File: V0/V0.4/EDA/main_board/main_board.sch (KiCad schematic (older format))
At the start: 24 parts, among them U1 top_rail_v2, U2 DS3231M, U3 INA219AxD, U5 KA78M05_TO252

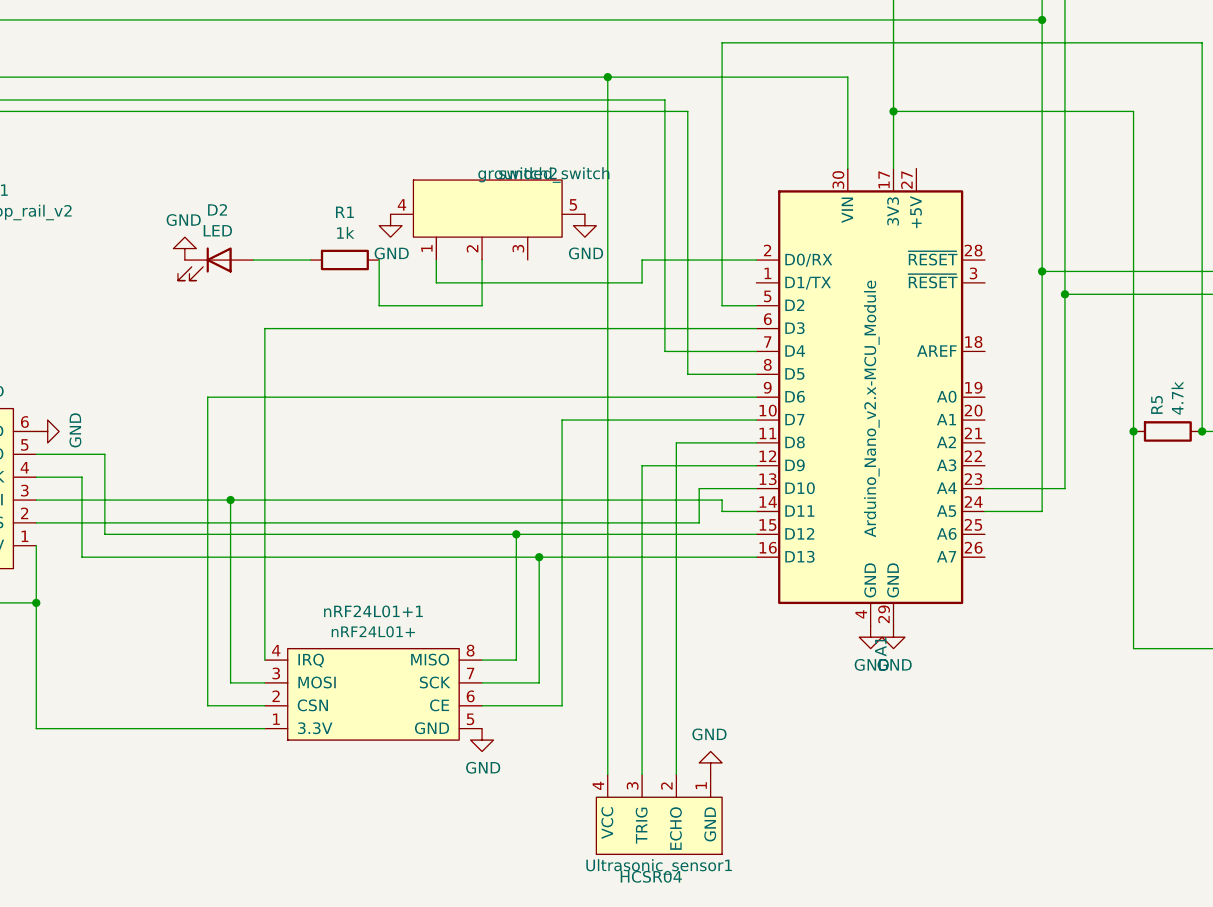
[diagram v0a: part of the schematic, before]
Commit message: update magnet_toggle.ino
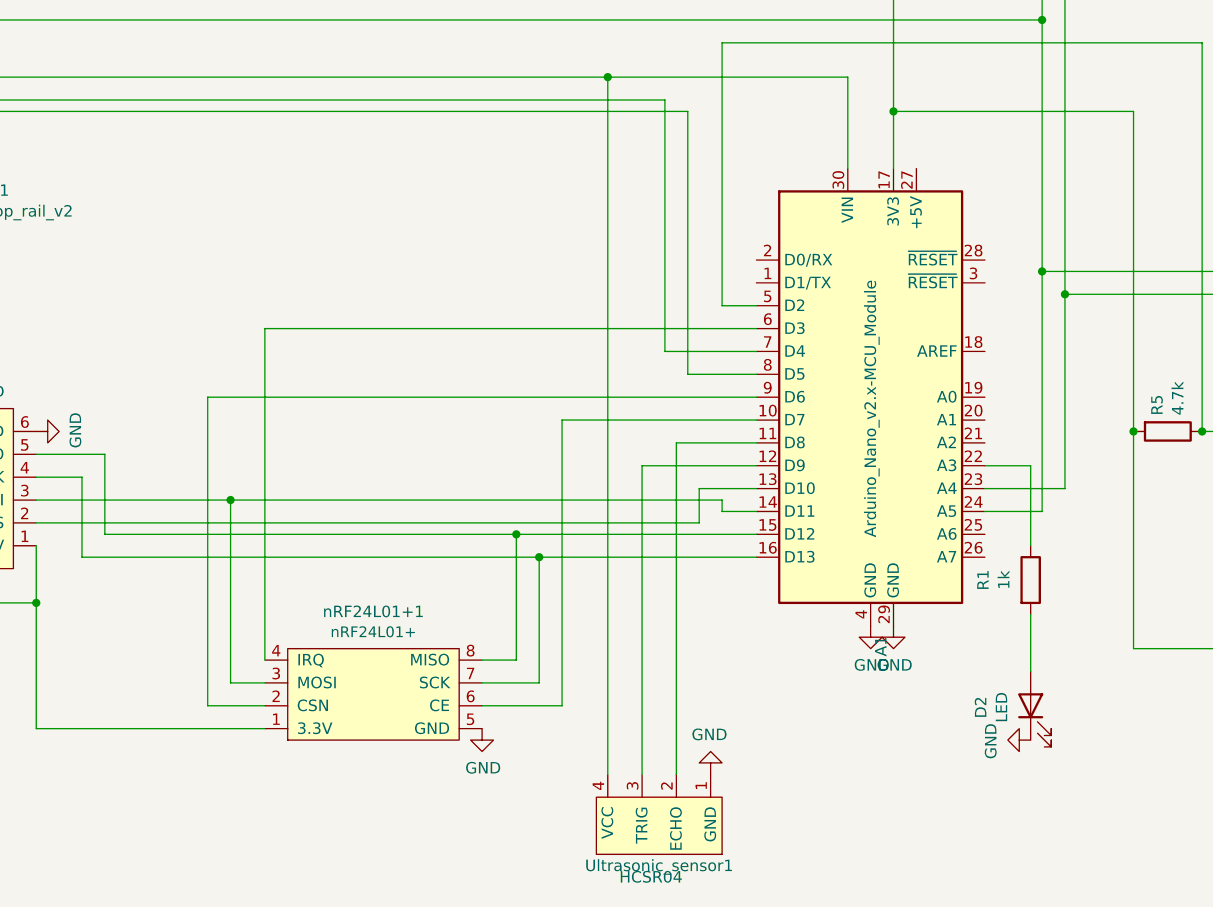
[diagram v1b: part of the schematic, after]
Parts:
- removed switch2: grounded_switch, ARTS-Lab:grounded_switch, symbol main_board-rescue:grounded_switch-whs5-rescue-whs5-rescue
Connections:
- net at A1.22 (A3): now also R1.1
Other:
- moved on the sheet: D2, R1
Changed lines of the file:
@@
 Wire Wire Line
 	6100 4450 6400 4450
-$Comp
-L Device:R R1
-U 1 1 60C43ADF
-P 4600 3950
-F 0 "R1" V 4393 3950 50  0000 C CNN
-F 1 "1k" V 4484 3950 50  0000 C CNN
-F 2 "Capacitor_SMD:C_1206_3216Metric_Pad1.42x1.75mm_HandSolder" V 4530 3950 50  0001 C CNN
-F 3 "~" H 4600 3950 50  0001 C CNN
-	1    4600 3950
-	0    1    1    0
-$EndComp
-$Comp
-L Device:LED D2
-U 1 1 60C4427C
-P 4050 3950
-F 0 "D2" H 4043 4167 50  0000 C CNN
-F 1 "LED" H 4043 4076 50  0000 C CNN
-F 2 "LED_THT:LED_D3.0mm" H 4050 3950 50  0001 C CNN
-F 3 "~" H 4050 3950 50  0001 C CNN
-	1    4050 3950
-	1    0    0    -1
-$EndComp
 Wire Wire Line
 	2200 5450 3250 5450
@@
 Wire Wire Line
 	6000 4350 6400 4350
-Wire Wire Line
-	4200 3950 4450 3950
 Wire Wire Line
 	2200 3000 2650 3000
@@
 $EndComp
 $Comp
-L power:GND #PWR010
-U 1 1 60B8EDF3
-P 3900 3950
-F 0 "#PWR010" H 3900 3700 50  0001 C CNN
-F 1 "GND" H 3905 3777 50  0000 C CNN
-F 2 "" H 3900 3950 50  0001 C CNN
-F 3 "" H 3900 3950 50  0001 C CNN
-	1    3900 3950
-	-1   0    0    1
-$EndComp
-$Comp
 L ARTS-Lab:top_rail_v2 U1
 U 1 1 60BDE75D
@@
 Wire Wire Line
 	4250 4250 6400 4250
-Wire Wire Line
-	4750 4150 5200 4150
-$Comp
-L power:GND #PWR017
-U 1 1 617507A6
-P 4800 3750
-F 0 "#PWR017" H 4800 3500 50  0001 C CNN
-F 1 "GND" H 4805 3577 50  0000 C CNN
-F 2 "" H 4800 3750 50  0001 C CNN
-F 3 "" H 4800 3750 50  0001 C CNN
-	1    4800 3750
-	1    0    0    -1
-$EndComp
-$Comp
-L power:GND #PWR018
-U 1 1 61751067
-P 5650 3750
-F 0 "#PWR018" H 5650 3500 50  0001 C CNN
-F 1 "GND" H 5655 3577 50  0000 C CNN
-F 2 "" H 5650 3750 50  0001 C CNN
-F 3 "" H 5650 3750 50  0001 C CNN
-	1    5650 3750
-	1    0    0    -1
-$EndComp
-Wire Wire Line
-	5200 3950 5200 4150
-Wire Wire Line
-	4750 3950 4750 4150
-Wire Wire Line
-	5000 3950 5000 4050
-Wire Wire Line
-	5000 4050 5900 4050
-Wire Wire Line
-	5900 4050 5900 3950
-Wire Wire Line
-	5900 3950 6400 3950
-$Comp
-L main_board-rescue:grounded_switch-whs5-rescue-whs5-rescue switch2
-U 1 1 6176D152
-P 5200 3600
-F 0 "switch2" H 5271 3627 50  0000 L CNN
-F 1 "grounded_switch" H 5180 3627 50  0000 L CNN
-F 2 "ARTS-Lab:grounded_switch" H 5200 3600 50  0001 C CNN
-F 3 "" H 5200 3600 50  0001 C CNN
-	1    5200 3600
-	1    0    0    -1
-$EndComp
+$Comp
+L power:GND #PWR010
+U 1 1 60B8EDF3
+P 7600 6050
+F 0 "#PWR010" H 7600 5800 50  0001 C CNN
+F 1 "GND" H 7605 5877 50  0000 C CNN
+F 2 "" H 7600 6050 50  0001 C CNN
+F 3 "" H 7600 6050 50  0001 C CNN
+	1    7600 6050
+	0    1    1    0
+$EndComp
+Wire Wire Line
+	7600 5750 7600 5500
+$Comp
+L Device:LED D2
+U 1 1 60C4427C
+P 7600 5900
+F 0 "D2" H 7593 6117 50  0000 C CNN
+F 1 "LED" H 7593 6026 50  0000 C CNN
+F 2 "LED_THT:LED_D3.0mm" H 7600 5900 50  0001 C CNN
+F 3 "~" H 7600 5900 50  0001 C CNN
+	1    7600 5900
+	0    -1   -1   0
+$EndComp
+$Comp
+L Device:R R1
+U 1 1 60C43ADF
+P 7600 5350
+F 0 "R1" V 7393 5350 50  0000 C CNN
+F 1 "1k" V 7484 5350 50  0000 C CNN
+F 2 "Capacitor_SMD:C_1206_3216Metric_Pad1.42x1.75mm_HandSolder" V 7530 5350 50  0001 C CNN
+F 3 "~" H 7600 5350 50  0001 C CNN
+	1    7600 5350
+	1    0    0    -1
+$EndComp
+Wire Wire Line
+	7400 4850 7600 4850
+Wire Wire Line
+	7600 4850 7600 5200
 $EndSCHEMATC
